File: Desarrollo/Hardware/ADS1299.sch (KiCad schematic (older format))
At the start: 31 parts, among them J2 I/O's Multi Propósito, U10 ADS1299, U14 OPA2376_NI

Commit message: Actualización de esquemático, se completaron campos de "Hoja de dato" y "Código Digikey" para cada componente. Se completaron los rótulos de hojas. Versión Final de PCB. Actualización de tamaño de pistas y redimensión de zonas de relleno. Lista de Materiales actualizada en carpeta "Documentación".
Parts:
- C36, C37: value NI -> 1uF
- C38: value NI -> 1nF
- JP5: value -AVSS -> AVSS(-)
- R19, R22, R23, R24: Código Digikey (none) -> 311-0.0ARCT-ND
- R20: Código Digikey (none) -> 311-390KARCT-ND
- R21: value NI -> 10k; Código Digikey (none) -> 311-10KARCT-ND
- U10: Código Digikey (none) -> 296-35009-ND
- U14: value OPA2376_NI -> OPA2376; Código Digikey (none) -> 296-22564-1-ND
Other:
- note added: "JP1: programación BIAS_DRV como BIAS_ELEC (1-2)\nJP2: referencia de malla de cable EEG (si posee)\nJP3: referencia eléctrica directa a SRB1 (2-3) o por buffer (1-2)\nJP4: electrodo de referencia a SRB2 (2-3) por buffer\nJP5: alimentación partida por conector hembra entre pines 2-3 (pin3: masa; pin2: -AVSS)"
- note removed: "(Usa CLK interno)"
- note removed: "Nota:\n\nNI: Not Installed"
- moved on the sheet: C19, C20, C38

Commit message: Revisión del SCH. Eliminación de JP5. Revisión de PCB y modificación de pistas basada en correción de errores del DRC. Se eliminaron todos los errores manteniendo el diseño. REVISAR. Además se quitaron las zonas de cobre debajo de los ADuM.
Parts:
- removed JP5: AVSS(-), Pin_Headers:Pin_Header_Straight_1x03, symbol JUMPER3
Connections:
- wire segments 195 -> 193
- no-connect marks 5 -> 4
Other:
- note added: "JP1: programación BIAS_DRV como BIAS_ELEC (1-2)\nJP2: referencia de malla de cable EEG (si posee)\nJP3: referencia eléctrica directa a SRB1 (2-3) o por buffer (1-2)\nJP4: electrodo de referencia a SRB2 (2-3) por buffer"
- note removed: "JP1: programación BIAS_DRV como BIAS_ELEC (1-2)\nJP2: referencia de malla de cable EEG (si posee)\nJP3: referencia eléctrica directa a SRB1 (2-3) o por buffer (1-2)\nJP4: electrodo de referencia a SRB2 (2-3) por buffer\nJP5: alimentación partida por conector hembra entre pines 2-3 (pin3: masa; pin2: -AVSS)"
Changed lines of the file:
@@
 Text Label 1800 1350 2    60   ~ 0
 BIAS_DRV
-$Comp
-L JUMPER3 JP5
-U 1 1 57CFEB0F
-P 1650 5500
-F 0 "JP5" H 1700 5400 50  0000 L CNN
-F 1 "AVSS(-)" H 1650 5600 50  0000 C BNN
-F 2 "Pin_Headers:Pin_Header_Straight_1x03" H 1650 5500 50  0001 C CNN
-F 3 "" H 1650 5500 50  0000 C CNN
-	1    1650 5500
-	-1   0    0    1
-$EndComp
-NoConn ~ 1900 5500
 Wire Wire Line
 	4400 2200 4600 2200
@@
 Connection ~ 1650 4750
 Wire Wire Line
-	1650 4550 1650 5400
-Wire Wire Line
 	1250 1500 1400 1500
 Wire Wire Line
@@
 Wire Wire Line
 	950  4750 1200 4750
-Wire Wire Line
-	1400 5500 1150 5500
-Wire Wire Line
-	1150 5500 1150 4750
-Connection ~ 1150 4750
 Wire Wire Line
 	6400 2600 6600 2600
@@
 Connection ~ 3950 4100
 Text Notes 850  6800 0    60   ~ 0
-JP1: programación BIAS_DRV como BIAS_ELEC (1-2)\nJP2: referencia de malla de cable EEG (si posee)\nJP3: referencia eléctrica directa a SRB1 (2-3) o por buffer (1-2)\nJP4: electrodo de referencia a SRB2 (2-3) por buffer\nJP5: alimentación partida por conector hembra entre pines 2-3 (pin3: masa; pin2: -AVSS)
+JP1: programación BIAS_DRV como BIAS_ELEC (1-2)\nJP2: referencia de malla de cable EEG (si posee)\nJP3: referencia eléctrica directa a SRB1 (2-3) o por buffer (1-2)\nJP4: electrodo de referencia a SRB2 (2-3) por buffer
 Wire Wire Line
 	3250 4100 3250 3800
@@
 Wire Wire Line
 	3100 5500 4400 5500
+Wire Wire Line
+	1650 4750 1650 4550
 $EndSCHEMATC

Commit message: Modificaciones basadas en nuevas revisiones. Se agregaron bypass en ADuMs. Inclusión de símbolos de "PONCHO" y "OPEN HARDWARE". Algunos cambios estéticos de pistas y otros funcionales. Unificación de vías. Extensión de capas de cobre en sector de aislación. Mejora de stitching. Quedaron revisiones pendientes que serán consultadas.
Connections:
- net labels added: DGND
- net labels removed: Earth
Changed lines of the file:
@@
 $EndComp
 $Comp
-L Earth #PWR013
+L DGND #PWR013
 U 1 1 57CB195C
 P 4500 5600
 F 0 "#PWR013" H 4500 5350 50  0001 C CNN
-F 1 "Earth" H 4500 5450 50  0001 C CNN
+F 1 "DGND" H 4500 5450 50  0001 C CNN
 F 2 "" H 4500 5600 50  0000 C CNN
 F 3 "" H 4500 5600 50  0000 C CNN
@@
 $EndComp
 $Comp
-L Earth #PWR014
+L DGND #PWR014
 U 1 1 57CB198A
 P 6500 5500
 F 0 "#PWR014" H 6500 5250 50  0001 C CNN
-F 1 "Earth" H 6500 5350 50  0001 C CNN
+F 1 "DGND" H 6500 5350 50  0001 C CNN
 F 2 "" H 6500 5500 50  0000 C CNN
 F 3 "" H 6500 5500 50  0000 C CNN
@@
 $EndComp
 $Comp
-L Earth #PWR015
+L DGND #PWR015
 U 1 1 57CB19B8
 P 7200 4500
 F 0 "#PWR015" H 7200 4250 50  0001 C CNN
-F 1 "Earth" H 7200 4350 50  0001 C CNN
+F 1 "DGND" H 7200 4350 50  0001 C CNN
 F 2 "" H 7200 4500 50  0000 C CNN
 F 3 "" H 7200 4500 50  0000 C CNN
@@
 $EndComp
 $Comp
-L Earth #PWR016
+L DGND #PWR016
 U 1 1 57CB19E6
 P 6650 3500
 F 0 "#PWR016" H 6650 3250 50  0001 C CNN
-F 1 "Earth" H 6650 3350 50  0001 C CNN
+F 1 "DGND" H 6650 3350 50  0001 C CNN
 F 2 "" H 6650 3500 50  0000 C CNN
 F 3 "" H 6650 3500 50  0000 C CNN
@@
 $EndComp
 $Comp
-L Earth #PWR017
+L DGND #PWR017
 U 1 1 57CB1A14
 P 9000 3100
 F 0 "#PWR017" H 9000 2850 50  0001 C CNN
-F 1 "Earth" H 9000 2950 50  0001 C CNN
+F 1 "DGND" H 9000 2950 50  0001 C CNN
 F 2 "" H 9000 3100 50  0000 C CNN
 F 3 "" H 9000 3100 50  0000 C CNN

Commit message: Actualización final con todas las revisiones corregidas. Realizar revisión FINAL.
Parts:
- removed J2: I/O's Multi Propósito, Pin_Headers:Pin_Header_Straight_1x04, symbol CONN_01X04
- added J2: IOs Multipropósito, Pin_Headers:Pin_Header_Straight_1x05, symbol CONN_01X05
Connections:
- wire segments 193 -> 195
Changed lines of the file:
@@
-	1    0    0    -1
-$EndComp
-$Comp
-L CONN_01X04 J2
-U 1 1 57C28EAE
-P 8600 3650
-F 0 "J2" H 8600 3900 50  0000 C CNN
-F 1 "I/O's Multi Propósito" V 8700 3650 50  0000 C CNN
-F 2 "Pin_Headers:Pin_Header_Straight_1x04" H 8600 3650 50  0001 C CNN
-F 3 "" H 8600 3650 50  0000 C CNN
-	1    8600 3650
 	1    0    0    -1
 $EndComp
@@
 	9400 5200 6400 5200
 Wire Wire Line
-	8400 3800 8300 3800
-Wire Wire Line
-	8300 3800 8300 4400
-Wire Wire Line
-	8400 3700 8200 3700
+	8300 3800 8550 3800
+Wire Wire Line
+	8300 4400 8300 3800
+Wire Wire Line
+	8200 3700 8550 3700
 Wire Wire Line
 	8200 3700 8200 4200
@@
 	8100 4100 8100 3600
 Wire Wire Line
-	8100 3600 8400 3600
-Wire Wire Line
-	8400 3500 8000 3500
+	8100 3600 8550 3600
+Wire Wire Line
+	8000 3500 8550 3500
 Wire Wire Line
 	8000 3500 8000 4000
@@
 Wire Wire Line
 	1650 4750 1650 4550
+$Comp
+L CONN_01X05 J2
+U 1 1 580DF4D4
+P 8750 3600
+F 0 "J2" H 8750 3900 50  0000 C CNN
+F 1 "IOs Multipropósito" V 8850 3600 50  0000 C CNN
+F 2 "Pin_Headers:Pin_Header_Straight_1x05" H 8750 3600 50  0001 C CNN
+F 3 "" H 8750 3600 50  0000 C CNN
+	1    8750 3600
+	1    0    0    -1
+$EndComp
+$Comp
+L DGND #PWR031
+U 1 1 580DF5E2
+P 8450 3900
+F 0 "#PWR031" H 8450 3650 50  0001 C CNN
+F 1 "DGND" H 8450 3750 50  0001 C CNN
+F 2 "" H 8450 3900 50  0000 C CNN
+F 3 "" H 8450 3900 50  0000 C CNN
+	1    8450 3900
+	1    0    0    -1
+$EndComp
+Wire Wire Line
+	8550 3400 8450 3400
+Wire Wire Line
+	8450 3400 8450 3900
 $EndSCHEMATC

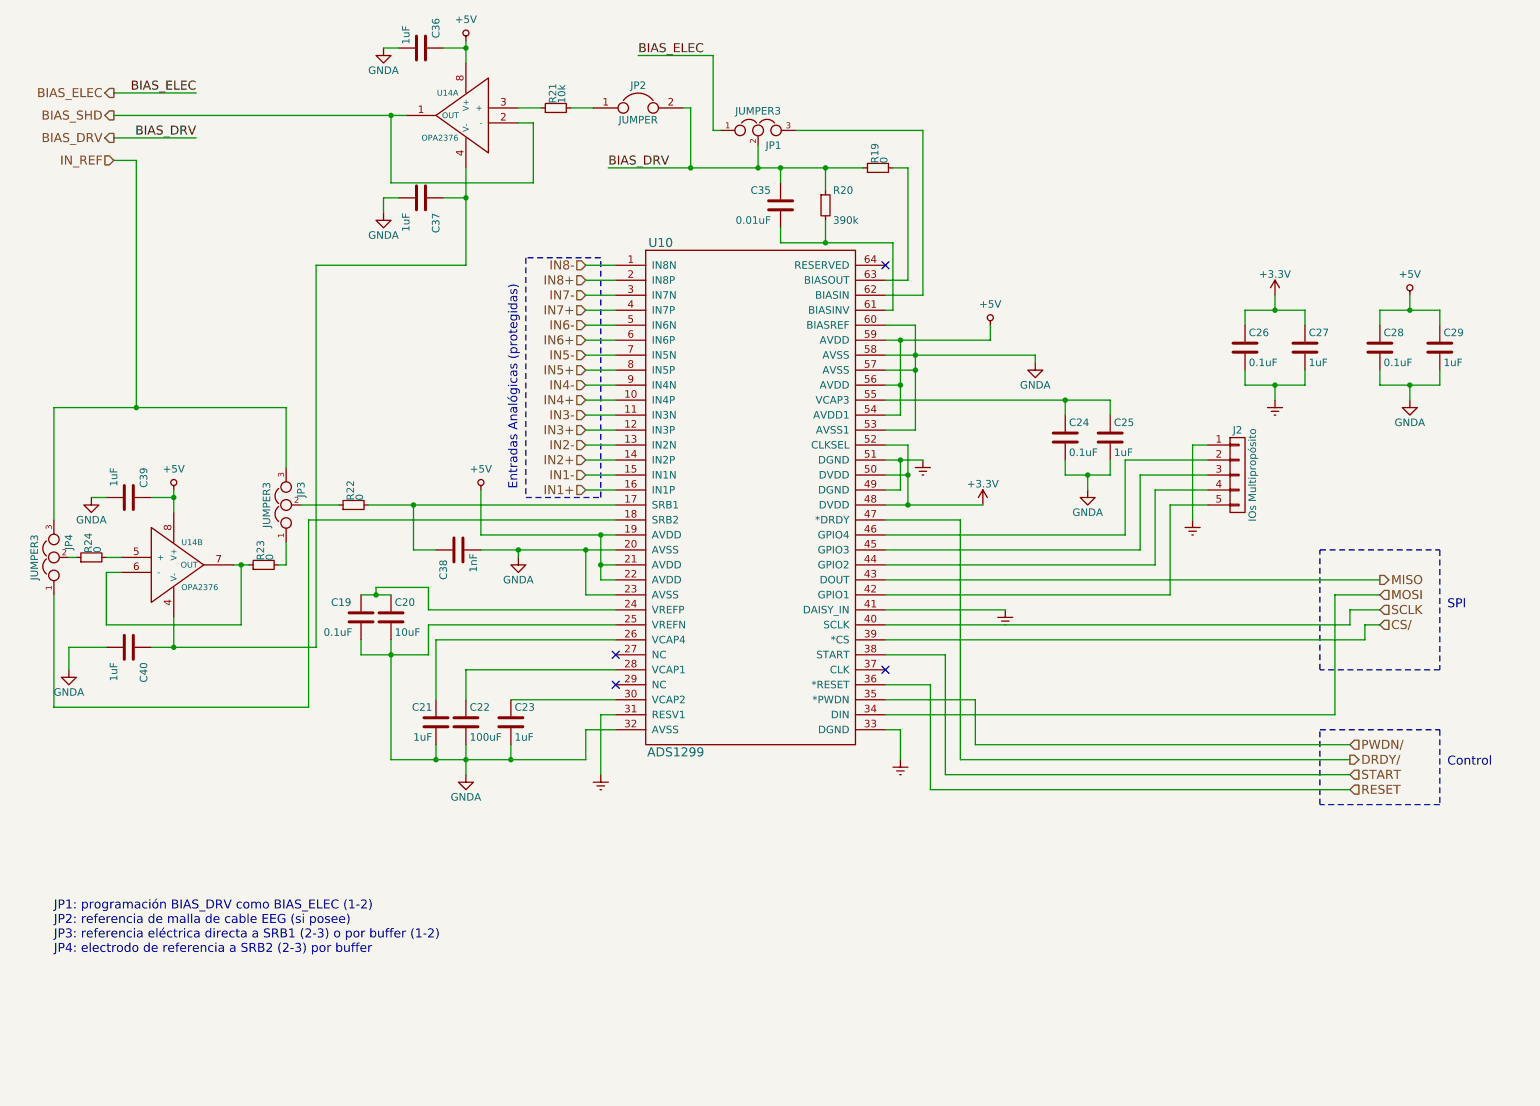
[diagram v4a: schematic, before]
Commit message: Nueva actualización. Intercambio de tierras GNDA por DGND en hoja esquemático "Aislación". Ídem en hoja de "Protección". Además se hizo visible el nombre de la tierra digital DGND que no figuraba. Revisión FINAL. Cambios estéticos en ubicación de algunas pistas del PCB.
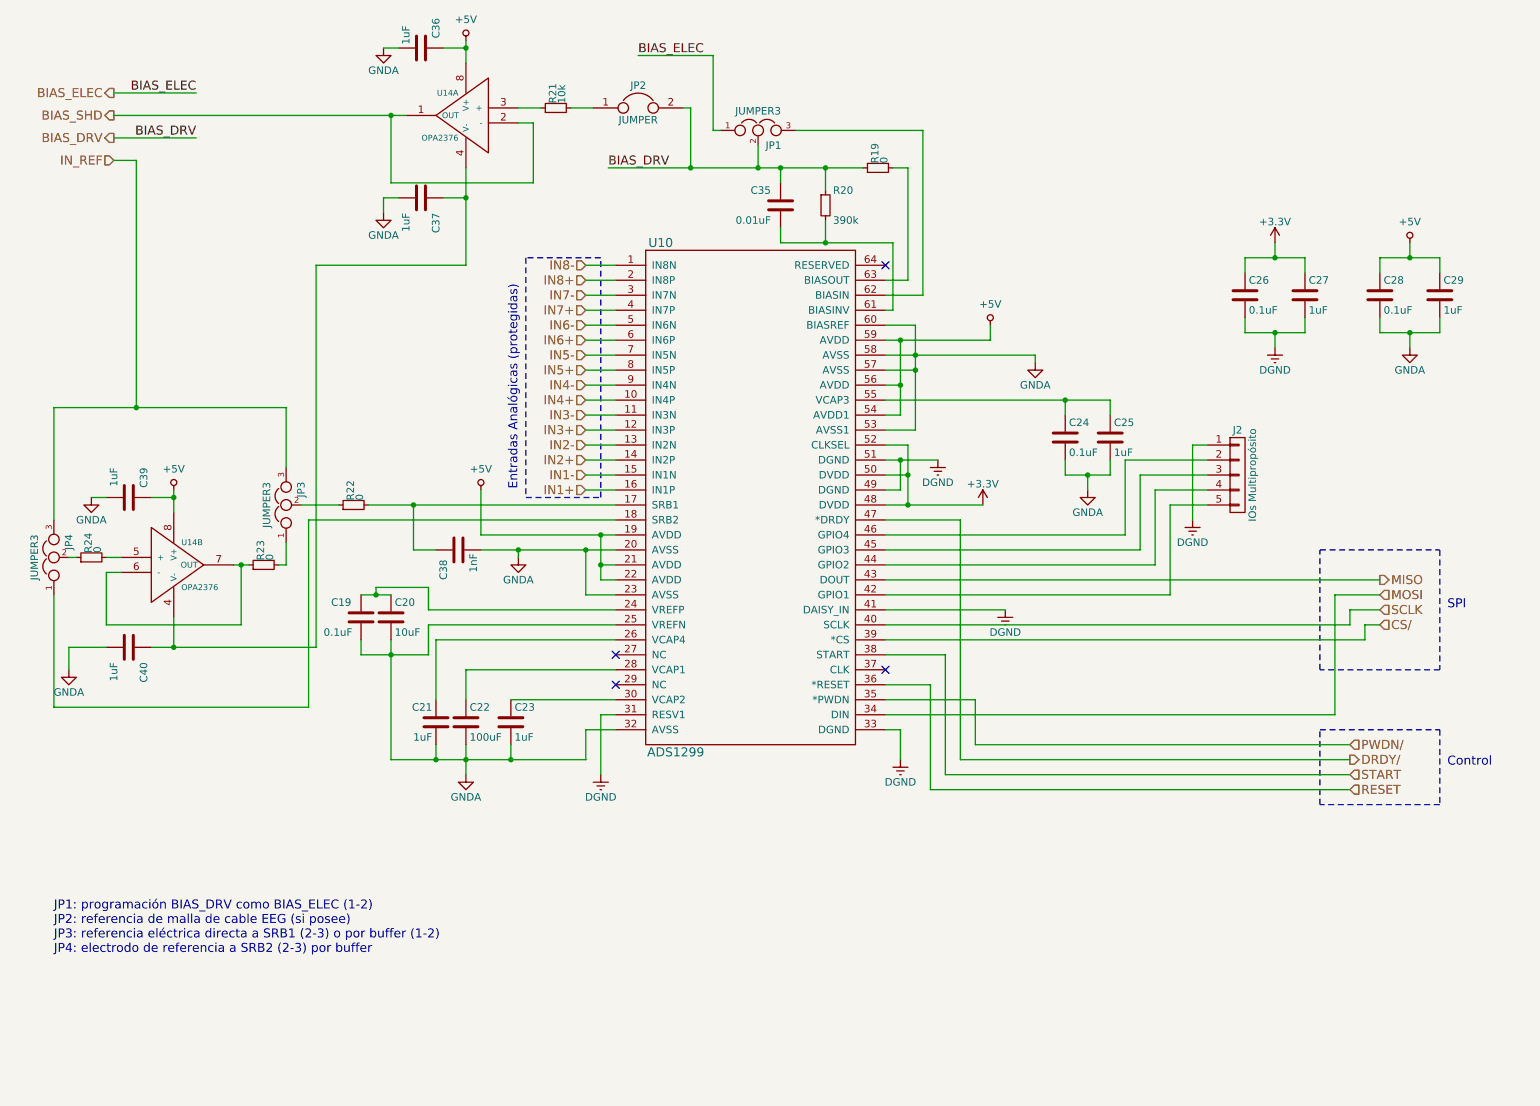
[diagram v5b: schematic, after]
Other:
- moved on the sheet: C26, C27, C28, C29
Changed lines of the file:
@@
 L C C26
 U 1 1 57C27C51
-P 8800 2750
-F 0 "C26" H 8825 2850 50  0000 L CNN
-F 1 "0.1uF" H 8825 2650 50  0000 L CNN
-F 2 "Capacitors_SMD:C_0805" H 8838 2600 50  0001 C CNN
-F 3 "http://www.kemet.com/Lists/ProductCatalog/Attachments/53/KEM_C1002_X7R_SMD.pdf" H 8800 2750 50  0001 C CNN
-	1    8800 2750
+P 8800 2400
+F 0 "C26" H 8825 2500 50  0000 L CNN
+F 1 "0.1uF" H 8825 2300 50  0000 L CNN
+F 2 "Capacitors_SMD:C_0805" H 8838 2250 50  0001 C CNN
+F 3 "http://www.kemet.com/Lists/ProductCatalog/Attachments/53/KEM_C1002_X7R_SMD.pdf" H 8800 2400 50  0001 C CNN
+	1    8800 2400
 	1    0    0    -1
 $EndComp
@@
 L C C27
 U 1 1 57C27C96
-P 9200 2750
-F 0 "C27" H 9225 2850 50  0000 L CNN
-F 1 "1uF" H 9225 2650 50  0000 L CNN
-F 2 "Capacitors_SMD:C_0805" H 9238 2600 50  0001 C CNN
-F 3 "http://www.kemet.com/Lists/ProductCatalog/Attachments/53/KEM_C1002_X7R_SMD.pdf" H 9200 2750 50  0001 C CNN
-	1    9200 2750
+P 9200 2400
+F 0 "C27" H 9225 2500 50  0000 L CNN
+F 1 "1uF" H 9225 2300 50  0000 L CNN
+F 2 "Capacitors_SMD:C_0805" H 9238 2250 50  0001 C CNN
+F 3 "http://www.kemet.com/Lists/ProductCatalog/Attachments/53/KEM_C1002_X7R_SMD.pdf" H 9200 2400 50  0001 C CNN
+	1    9200 2400
 	1    0    0    -1
 $EndComp
@@
 L C C28
 U 1 1 57C27CC9
-P 9700 2750
-F 0 "C28" H 9725 2850 50  0000 L CNN
-F 1 "0.1uF" H 9725 2650 50  0000 L CNN
-F 2 "Capacitors_SMD:C_0805" H 9738 2600 50  0001 C CNN
-F 3 "http://www.kemet.com/Lists/ProductCatalog/Attachments/53/KEM_C1002_X7R_SMD.pdf" H 9700 2750 50  0001 C CNN
-	1    9700 2750
+P 9700 2400
+F 0 "C28" H 9725 2500 50  0000 L CNN
+F 1 "0.1uF" H 9725 2300 50  0000 L CNN
+F 2 "Capacitors_SMD:C_0805" H 9738 2250 50  0001 C CNN
+F 3 "http://www.kemet.com/Lists/ProductCatalog/Attachments/53/KEM_C1002_X7R_SMD.pdf" H 9700 2400 50  0001 C CNN
+	1    9700 2400
 	1    0    0    -1
 $EndComp
@@
 L C C29
 U 1 1 57C27CFC
-P 10100 2750
-F 0 "C29" H 10125 2850 50  0000 L CNN
-F 1 "1uF" H 10125 2650 50  0000 L CNN
-F 2 "Capacitors_SMD:C_0805" H 10138 2600 50  0001 C CNN
-F 3 "http://www.kemet.com/Lists/ProductCatalog/Attachments/53/KEM_C1002_X7R_SMD.pdf" H 10100 2750 50  0001 C CNN
-	1    10100 2750
+P 10100 2400
+F 0 "C29" H 10125 2500 50  0000 L CNN
+F 1 "1uF" H 10125 2300 50  0000 L CNN
+F 2 "Capacitors_SMD:C_0805" H 10138 2250 50  0001 C CNN
+F 3 "http://www.kemet.com/Lists/ProductCatalog/Attachments/53/KEM_C1002_X7R_SMD.pdf" H 10100 2400 50  0001 C CNN
+	1    10100 2400
 	1    0    0    -1
 $EndComp
@@
 L +3.3V-RESCUE-PonchoERG #PWR?
 U 1 1 57CB18B2
-P 9000 2400
+P 9000 2050
 AR Path="/57CB18B2" Ref="#PWR?"  Part="1"
 AR Path="/57BDC369/57CB18B2" Ref="#PWR011"  Part="1"
-F 0 "#PWR011" H 9000 2250 50  0001 C CNN
-F 1 "+3.3V" H 9000 2540 50  0000 C CNN
-F 2 "" H 9000 2400 50  0000 C CNN
-F 3 "" H 9000 2400 50  0000 C CNN
-	1    9000 2400
+F 0 "#PWR011" H 9000 1900 50  0001 C CNN
+F 1 "+3.3V" H 9000 2190 50  0000 C CNN
+F 2 "" H 9000 2050 50  0000 C CNN
+F 3 "" H 9000 2050 50  0000 C CNN
+	1    9000 2050
 	1    0    0    -1
 $EndComp
@@
 L +5V #PWR012
 U 1 1 57CB18ED
-P 9900 2400
-F 0 "#PWR012" H 9900 2250 50  0001 C CNN
-F 1 "+5V" H 9900 2540 50  0000 C CNN
-F 2 "" H 9900 2400 50  0000 C CNN
-F 3 "" H 9900 2400 50  0000 C CNN
-	1    9900 2400
+P 9900 2050
+F 0 "#PWR012" H 9900 1900 50  0001 C CNN
+F 1 "+5V" H 9900 2190 50  0000 C CNN
+F 2 "" H 9900 2050 50  0000 C CNN
+F 3 "" H 9900 2050 50  0000 C CNN
+	1    9900 2050
 	1    0    0    -1
 $EndComp
@@
 P 4500 5600
 F 0 "#PWR013" H 4500 5350 50  0001 C CNN
-F 1 "DGND" H 4500 5450 50  0001 C CNN
+F 1 "DGND" H 4500 5450 50  0000 C CNN
 F 2 "" H 4500 5600 50  0000 C CNN
 F 3 "" H 4500 5600 50  0000 C CNN
@@
 P 6500 5500
 F 0 "#PWR014" H 6500 5250 50  0001 C CNN
-F 1 "DGND" H 6500 5350 50  0001 C CNN
+F 1 "DGND" H 6500 5350 50  0000 C CNN
 F 2 "" H 6500 5500 50  0000 C CNN
 F 3 "" H 6500 5500 50  0000 C CNN
@@
 P 7200 4500
 F 0 "#PWR015" H 7200 4250 50  0001 C CNN
-F 1 "DGND" H 7200 4350 50  0001 C CNN
+F 1 "DGND" H 7200 4350 50  0000 C CNN
 F 2 "" H 7200 4500 50  0000 C CNN
 F 3 "" H 7200 4500 50  0000 C CNN
@@
 L DGND #PWR016
 U 1 1 57CB19E6
-P 6650 3500
-F 0 "#PWR016" H 6650 3250 50  0001 C CNN
-F 1 "DGND" H 6650 3350 50  0001 C CNN
-F 2 "" H 6650 3500 50  0000 C CNN
-F 3 "" H 6650 3500 50  0000 C CNN
-	1    6650 3500
+P 6750 3500
+F 0 "#PWR016" H 6750 3250 50  0001 C CNN
+F 1 "DGND" H 6750 3350 50  0000 C CNN
+F 2 "" H 6750 3500 50  0000 C CNN
+F 3 "" H 6750 3500 50  0000 C CNN
+	1    6750 3500
 	1    0    0    -1
 $EndComp
@@
 L DGND #PWR017
 U 1 1 57CB1A14
-P 9000 3100
-F 0 "#PWR017" H 9000 2850 50  0001 C CNN
-F 1 "DGND" H 9000 2950 50  0001 C CNN
-F 2 "" H 9000 3100 50  0000 C CNN
-F 3 "" H 9000 3100 50  0000 C CNN
-	1    9000 3100
+P 9000 2750
+F 0 "#PWR017" H 9000 2500 50  0001 C CNN
+F 1 "DGND" H 9000 2600 50  0000 C CNN
+F 2 "" H 9000 2750 50  0000 C CNN
+F 3 "" H 9000 2750 50  0000 C CNN
+	1    9000 2750
 	1    0    0    -1
 $EndComp
@@
 L GNDA-RESCUE-PonchoERG #PWR019
 U 1 1 57CB1AB1
-P 9900 3100
-F 0 "#PWR019" H 9900 2850 50  0001 C CNN
-F 1 "GNDA" H 9900 2950 50  0000 C CNN
-F 2 "" H 9900 3100 50  0000 C CNN
-F 3 "" H 9900 3100 50  0000 C CNN
-	1    9900 3100
+P 9900 2750
+F 0 "#PWR019" H 9900 2500 50  0001 C CNN
+F 1 "GNDA" H 9900 2600 50  0000 C CNN
+F 2 "" H 9900 2750 50  0000 C CNN
+F 3 "" H 9900 2750 50  0000 C CNN
+	1    9900 2750
 	1    0    0    -1
 $EndComp
@@
 Connection ~ 6500 3500
 Wire Wire Line
-	6400 3500 6650 3500
+	6400 3500 6750 3500
 Wire Wire Line
 	7200 4500 6400 4500
 Wire Wire Line
-	9000 3100 9000 3000
-Wire Wire Line
-	8800 3000 9200 3000
-Wire Wire Line
-	8800 3000 8800 2900
-Wire Wire Line
-	8800 2600 8800 2500
-Wire Wire Line
-	8800 2500 9200 2500
-Wire Wire Line
-	9000 2500 9000 2400
-Wire Wire Line
-	9200 2500 9200 2600
-Connection ~ 9000 2500
-Wire Wire Line
-	9200 3000 9200 2900
-Connection ~ 9000 3000
-Wire Wire Line
-	9900 3100 9900 3000
-Wire Wire Line
-	9700 3000 10100 3000
-Wire Wire Line
-	9700 3000 9700 2900
-Wire Wire Line
-	10100 3000 10100 2900
-Connection ~ 9900 3000
-Wire Wire Line
-	10100 2500 10100 2600
-Wire Wire Line
-	9700 2500 10100 2500
-Wire Wire Line
-	9900 2500 9900 2400
-Wire Wire Line
-	9700 2500 9700 2600
-Connection ~ 9900 2500
+	9000 2750 9000 2650
+Wire Wire Line
+	8800 2650 9200 2650
+Wire Wire Line
+	8800 2650 8800 2550
+Wire Wire Line
+	8800 2250 8800 2150
+Wire Wire Line
+	8800 2150 9200 2150
+Wire Wire Line
+	9000 2150 9000 2050
+Wire Wire Line
+	9200 2150 9200 2250
+Connection ~ 9000 2150
+Wire Wire Line
+	9200 2650 9200 2550
+Connection ~ 9000 2650
+Wire Wire Line
+	9900 2750 9900 2650
+Wire Wire Line
+	9700 2650 10100 2650
+Wire Wire Line
+	9700 2650 9700 2550
+Wire Wire Line
+	10100 2650 10100 2550
+Connection ~ 9900 2650
+Wire Wire Line
+	10100 2150 10100 2250
+Wire Wire Line
+	9700 2150 10100 2150
+Wire Wire Line
+	9900 2150 9900 2050
+Wire Wire Line
+	9700 2150 9700 2250
+Connection ~ 9900 2150
 Wire Wire Line
 	6400 4400 8300 4400
@@
 P 8450 3900
 F 0 "#PWR031" H 8450 3650 50  0001 C CNN
-F 1 "DGND" H 8450 3750 50  0001 C CNN
+F 1 "DGND" H 8450 3750 50  0000 C CNN
 F 2 "" H 8450 3900 50  0000 C CNN
 F 3 "" H 8450 3900 50  0000 C CNN

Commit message: Actualización final. Serigrafía nueva de jumpers y logos que se habían borrado de PONCHO y OPEN HARDWARE. PLACA TERMINADA.
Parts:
- added Jumper_Config1: J_CFG, footprints:Jumpers_Default, symbol J_CFG
- added Jumper_STD1: J_STD, footprints:Jumpers_Default, symbol J_STD
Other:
- note added: "1-2"
- note added: "2-3"
- note added: "Buffer"
- note added: "Conexión malla (shield) cable paciente"
- note added: "Configuración Default (PCB)"
- note added: "Configuración JP3-JP4"
- note added: "IN_REF a SRB1 por buffer"
- note added: "IN_REF directo SRB1 (Default)"
- note added: "IN_REF por buffer (Default)"
- note added: "Indistinto"
- note added: "JP1"
- note added: "JP2"
- note added: "JP3"
- note added: "JP4"
- note added: "No Conectado (Default)"
- note added: "Programación BIAS_DRV como BIAS_ELEC"
- note added: "Programación interna BIAS"
- note added: "Set de Configuración (PCB)"
- note added: "Sin Buffer"
- note removed: "JP1: programación BIAS_DRV como BIAS_ELEC (1-2)\nJP2: referencia de malla de cable EEG (si posee)\nJP3: referencia eléctrica directa a SRB1 (2-3) o por buffer (1-2)\nJP4: electrodo de referencia a SRB2 (2-3) por buffer"
